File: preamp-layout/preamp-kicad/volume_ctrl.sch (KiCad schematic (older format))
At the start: 72 parts, among them J64 Conn_01x05_Male, J65 Conn_01x02_Male, J66 Conn_01x02_Male, J67 Conn_01x03_Female, J68 Conn_01x03_Female, J69 Conn_01x03_Male, J70 Conn_01x03_Male, J71 Conn_01x03_Male, U10 MCP4902, U11 TL072, U12 TL072, U13 THAT2181, U14 THAT2181, U15 TL072, U16 THAT2181, U17 THAT2181, U18 TL072, U9 MCP4902

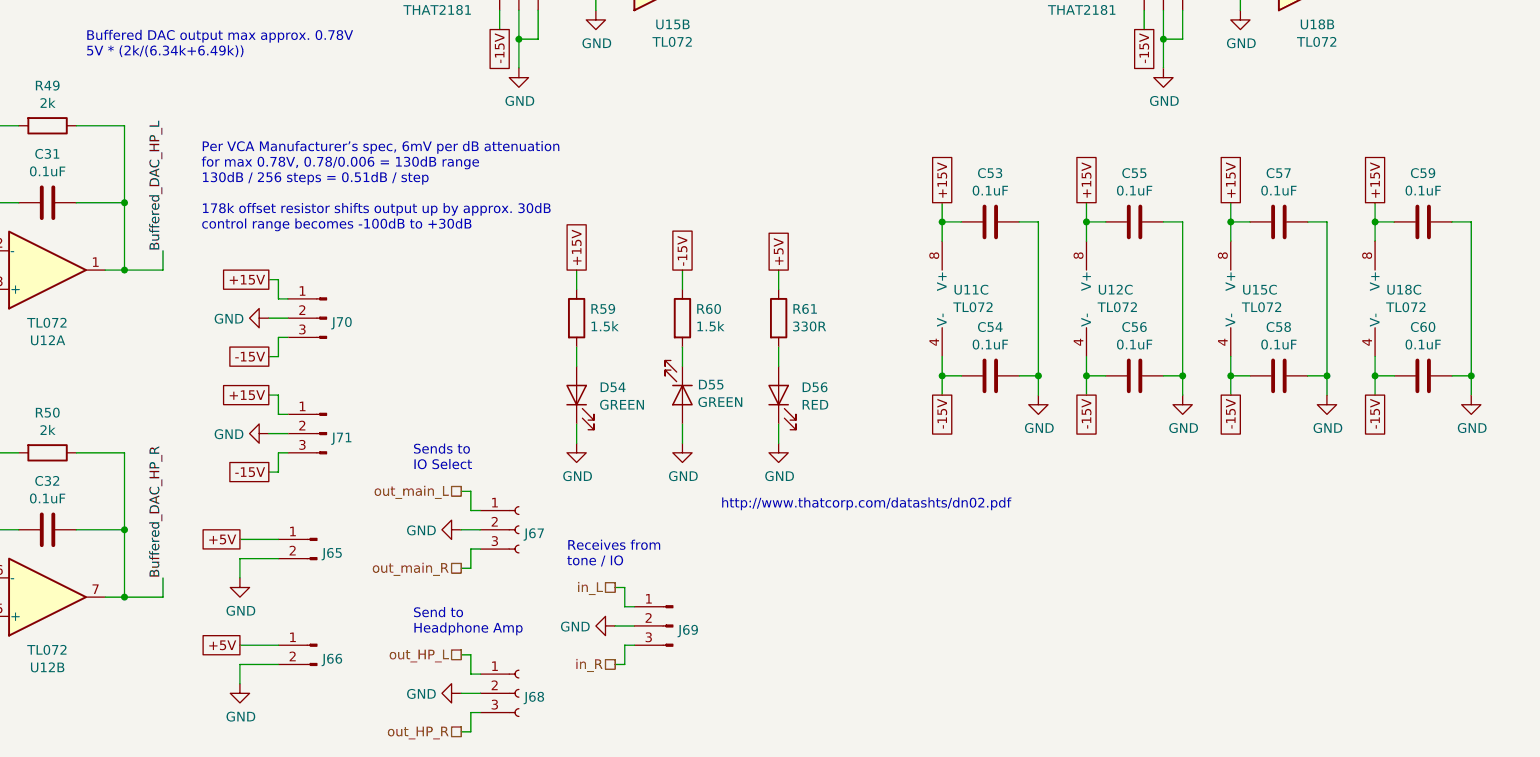
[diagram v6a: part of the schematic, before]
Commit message: Headphone Amp Update
Removed IC buffer on headphone amp schematic. Reconfigured connectors to crossfeed board so that input/output can be easily jumpered.
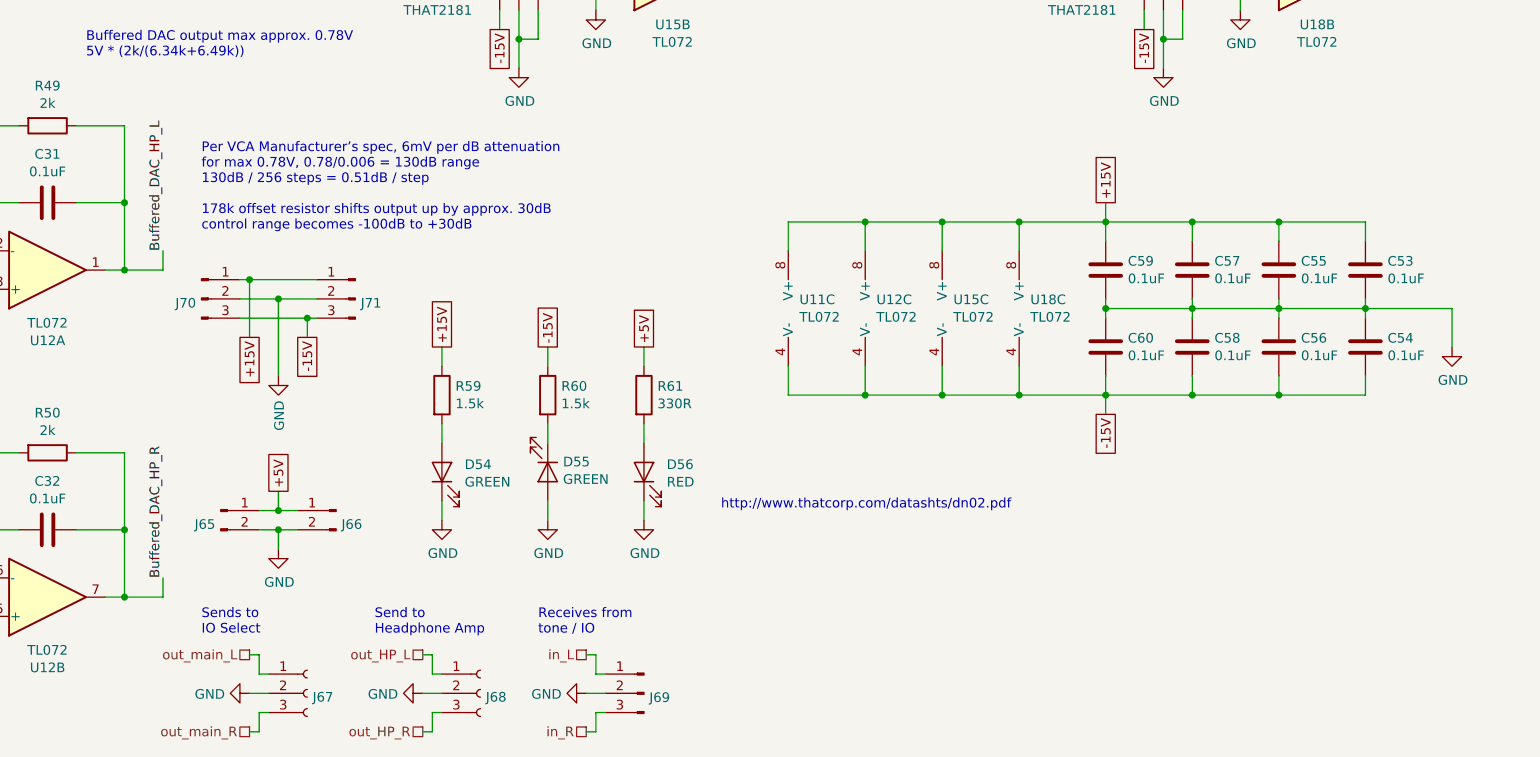
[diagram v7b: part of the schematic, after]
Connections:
- net -15V: now also C54.2, C56.2, C58.2, C60.2; no longer C54.1, C56.1, C58.1, C60.1
- net GND: now also C54.1, C56.1, C58.1, C60.1; no longer C54.2, C56.2, C58.2, C60.2
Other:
- moved on the sheet: C53, C54, C55, C56, C57, C58, C59, C60, D54, D55, D56, J65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

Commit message: Footprint updates
Footprint creation of relay, ESP32
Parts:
- U10, U9: footprint (none) -> Package_SO:SOIC-14_3.9x8.7mm_P1.27mm
- U13, U14, U16, U17: footprint (none) -> Package_SO:SO-8_3.9x4.9mm_P1.27mm
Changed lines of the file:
@@
 F 0 "U13" H 5450 1400 50  0000 L CNN
 F 1 "THAT2181" H 5350 1300 50  0000 L CNN
-F 2 "" H 5950 1600 50  0001 C CNN
+F 2 "Package_SO:SO-8_3.9x4.9mm_P1.27mm" H 5950 1600 50  0001 C CNN
 F 3 "http://www.thatcorp.com/datashts/THAT_2181-Series_Datasheet.pdf" H 5950 1600 50  0001 C CNN
 	1    5950 1600
@@
 F 0 "U14" H 5450 3400 50  0000 L CNN
 F 1 "THAT2181" H 5350 3300 50  0000 L CNN
-F 2 "" H 5950 3600 50  0001 C CNN
+F 2 "Package_SO:SO-8_3.9x4.9mm_P1.27mm" H 5950 3600 50  0001 C CNN
 F 3 "http://www.thatcorp.com/datashts/THAT_2181-Series_Datasheet.pdf" H 5950 3600 50  0001 C CNN
 	1    5950 3600
@@
 F 0 "U10" H 1700 6400 50  0000 C CNN
 F 1 "MCP4902" H 1700 6300 50  0000 C CNN
-F 2 "" H 2300 5650 50  0001 C CNN
+F 2 "Package_SO:SOIC-14_3.9x8.7mm_P1.27mm" H 2300 5650 50  0001 C CNN
 F 3 "http://ww1.microchip.com/downloads/en/DeviceDoc/22250A.pdf" H 2300 5650 50  0001 C CNN
 	1    1500 5950
@@
 F 0 "U16" H 8800 1400 50  0000 L CNN
 F 1 "THAT2181" H 8700 1300 50  0000 L CNN
-F 2 "" H 9300 1600 50  0001 C CNN
+F 2 "Package_SO:SO-8_3.9x4.9mm_P1.27mm" H 9300 1600 50  0001 C CNN
 F 3 "http://www.thatcorp.com/datashts/THAT_2181-Series_Datasheet.pdf" H 9300 1600 50  0001 C CNN
 	1    9300 1600
@@
 F 0 "U17" H 8800 3400 50  0000 L CNN
 F 1 "THAT2181" H 8700 3300 50  0000 L CNN
-F 2 "" H 9300 3600 50  0001 C CNN
+F 2 "Package_SO:SO-8_3.9x4.9mm_P1.27mm" H 9300 3600 50  0001 C CNN
 F 3 "http://www.thatcorp.com/datashts/THAT_2181-Series_Datasheet.pdf" H 9300 3600 50  0001 C CNN
 	1    9300 3600
@@
 F 0 "U9" H 1700 2900 50  0000 C CNN
 F 1 "MCP4902" H 1700 2800 50  0000 C CNN
-F 2 "" H 2300 2150 50  0001 C CNN
+F 2 "Package_SO:SOIC-14_3.9x8.7mm_P1.27mm" H 2300 2150 50  0001 C CNN
 F 3 "http://ww1.microchip.com/downloads/en/DeviceDoc/22250A.pdf" H 2300 2150 50  0001 C CNN
 	1    1500 2450
